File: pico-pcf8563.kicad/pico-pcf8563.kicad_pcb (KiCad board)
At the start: 2 copper layers, 21 x 18.6 mm, 13 parts, among them J1 Stemma-QT_Qwicc, J2 Ext_Conn, J4 Pico Pin 1-7, J5 Pico Pin 40-34, U1 PCF8563T, Y1 Crystal

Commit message: Rev2
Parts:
- added JP2: ~{INT}_Jumper, Jumper:SolderJumper-2_P1.3mm_Bridged_Pad1.0x1.5mm, B.Cu at (114.5, 109.5)
- added JP3: COUT_Jumper, Jumper:SolderJumper-2_P1.3mm_Bridged_Pad1.0x1.5mm, B.Cu at (114.5, 112.1)
- JP1: value VDD_SEL -> 3V3_Jumper; footprint Jumper:SolderJumper-3_P1.3mm_Bridged12_Pad1.0x1.5mm -> Jumper:SolderJumper-2_P1.3mm_Bridged_Pad1.0x1.5mm; moved to B.Cu
- moved R3 5.03 mm to (104.2, 112.4)
- moved R2 2.77 mm to (113.4, 100.5), turned to 90 degrees
- moved JP1 2.62 mm to (102.7, 108.7), turned to 90 degrees
- moved Y1 0.73 mm to (103.9, 102.2)
- moved C1 0.41 mm to (111.7, 100.0), turned to 180 degrees
- moved C2 0.38 mm to (106.1, 100.0)
- moved J1 0.33 mm to (108.9, 110.5)
- moved J2 0.33 mm to (102.5, 115.2)
- moved U1 0.33 mm to (108.9, 103.4)
- moved R1 0.26 mm to (115.2, 110.0)
- moved R4 0.20 mm to (115.2, 107.6)
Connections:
- C1 pad 1: VDD -> VCC
- J4 pad 6: unconnected-(J4-Pad6) -> /GP4
- J4 pad 7: unconnected-(J4-Pad7) -> /GP5
- JP1 pad 2: VDD -> VCC
- R2 pad 2: VDD -> VCC
- R3 pad 2: VDD -> VCC
- U1 pad 8: VDD -> VCC
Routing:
- net VDD: track 22.3 -> 0.00 mm
- net VCC: track 10.6 -> 32.1 mm, vias 0 -> 2
- net +3V3: track 3.07 -> 18.2 mm, vias 0 -> 1
- net /~{INT}: track 16.4 -> 25.7 mm
- net /SCL: track 19.9 -> 28.0 mm, vias 0 -> 1
- net GND: track 0.00 -> 7.26 mm, vias 0 -> 3
- net /COUT: track 15.7 -> 20.6 mm, vias 1 -> 2
- net /SDA: track 14.9 -> 19.4 mm
- net /GP4: track 0.00 -> 4.45 mm
- net /GP5: track 0.00 -> 4.23 mm
- added copper zone on B.Cu, net GND
- added copper zone on F.Cu, net GND

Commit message: Rev 3
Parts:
- J4: moved to B.Cu
- moved R1 4.33 mm to (114.6, 105.7), turned to -90 degrees
- moved R4 2.69 mm to (113.3, 105.7), turned to 90 degrees
- turned J4 to 180 degrees
- turned JP1 to -90 degrees
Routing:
- net +3V3: track 18.2 -> 45.4 mm, vias 1 -> 0
- net VCC: track 32.1 -> 57.8 mm, vias 2 -> 1
- net GND: track 7.26 -> 14.0 mm
- net /SCL: track 28.0 -> 25.6 mm
- net /SDA: track 19.4 -> 18.5 mm
- net /~{INT}: track 25.7 -> 25.1 mm
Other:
- board text added: "3V3 VCC"
- board text added: "COUT"
- board text added: "G"
- board text added: "SCL"
- board text added: "SDA"
- board text added: "VCC"
- board text added: "github.com/bablokb/ pcb-pico-pcf8563 Rev 3"
- board text added: "~{INT}"

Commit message: updated pcb from schematic for Rev3
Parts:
- JP2: value ~{INT}_Jumper -> COUT_Jumper
- JP3: value COUT_Jumper -> ~{INT}_Jumper
- R2: value 100K -> 10K
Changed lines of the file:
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@@
       (layerselection 0x00010fc_ffffffff)
       (disableapertmacros false)
-      (usegerberextensions false)
-      (usegerberattributes true)
-      (usegerberadvancedattributes true)
-      (creategerberjobfile true)
+      (usegerberextensions true)
+      (usegerberattributes false)
+      (usegerberadvancedattributes false)
+      (creategerberjobfile false)
       (svguseinch false)
       (svgprecision 6)
@@
       (psa4output false)
       (plotreference true)
-      (plotvalue true)
+      (plotvalue false)
       (plotinvisibletext false)
       (sketchpadsonfab false)
-      (subtractmaskfromsilk false)
+      (subtractmaskfromsilk true)
       (outputformat 1)
       (mirror false)
-      (drillshape 1)
+      (drillshape 0)
       (scaleselection 1)
-      (outputdirectory "")
+      (outputdirectory "../jlcpcb")
     )
   )
@@
     (descr "Resistor SMD 0402 (1005 Metric), square (rectangular) end terminal, IPC_7351 nominal, (Body size source: IPC-SM-782 page 72, https://www.pcb-3d.com/wordpress/wp-content/uploads/ipc-sm-782a_amendment_1_and_2.pdf), generated with kicad-footprint-generator")
     (tags "resistor")
-    (property "LCSC" "C25741")
+    (property "LCSC" "C25744")
     (property "Sheetfile" "pico-pcf8563.kicad_sch")
     (property "Sheetname" "")
@@
       (effects (font (size 1 1) (thickness 0.15)))
     )
-    (fp_text value "100K" (at 0 1.17 90) (layer "F.Fab") hide
+    (fp_text value "10K" (at 0 1.17 90) (layer "F.Fab") hide
       (effects (font (size 1 1) (thickness 0.15)))
     )
@@
     (property "Sheetname" "")
     (property "Value" "Stemma-QT_Qwicc")
-    (attr smd)
+    (attr smd exclude_from_pos_files)
     (fp_text reference "J1" (at 0 0) (layer "F.SilkS") hide
       (effects (font (size 1 1) (thickness 0.15)))
@@
     (pad "4" smd roundrect (at 1.5 -2) (size 0.6 1.55) (layers "F.Cu" "F.Paste" "F.Mask") (roundrect_rratio 0.25)
       (net 6 "/SCL") (pinfunction "SCL") (pintype "bidirectional"))
-    (pad "MP" smd roundrect (at -2.8 1.875) (size 1.2 1.8) (layers "F.Cu" "F.Paste" "F.Mask") (roundrect_rratio 0.208333))
-    (pad "MP" smd roundrect (at 2.8 1.875) (size 1.2 1.8) (layers "F.Cu" "F.Paste" "F.Mask") (roundrect_rratio 0.208333))
+    (pad "MP" smd roundrect (at -2.8 1.875) (size 1.2 1.8) (layers "F.Cu" "F.Paste" "F.Mask") (roundrect_rratio 0.2083333333))
+    (pad "MP" smd roundrect (at 2.8 1.875) (size 1.2 1.8) (layers "F.Cu" "F.Paste" "F.Mask") (roundrect_rratio 0.2083333333))
     (model "${KICAD6_3DMODEL_DIR}/Connector_JST.3dshapes/JST_SH_SM04B-SRSS-TB_1x04-1MP_P1.00mm_Horizontal.wrl"
       (offset (xyz 0 0 0))
@@
       (effects (font (size 1 1) (thickness 0.15)) (justify mirror))
     )
-    (fp_text value "~{INT}_Jumper" (at 0 -1.9) (layer "B.Fab") hide
+    (fp_text value "COUT_Jumper" (at 0 -1.9) (layer "B.Fab") hide
       (effects (font (size 1 1) (thickness 0.15)) (justify mirror))
     )
@@
       (effects (font (size 1 1) (thickness 0.15)) (justify mirror))
     )
-    (fp_text value "COUT_Jumper" (at 0 -1.9) (layer "B.Fab") hide
-      (effects (font (size 1 1) (thickness 0.15)) (justify mirror))
-    )
+    (fp_text value "~{INT}_Jumper" (at 0 -1.9) (layer "B.Fab") hide
+      (effects (font (size 1 1) (thickness 0.15)) (justify mirror))
+    )

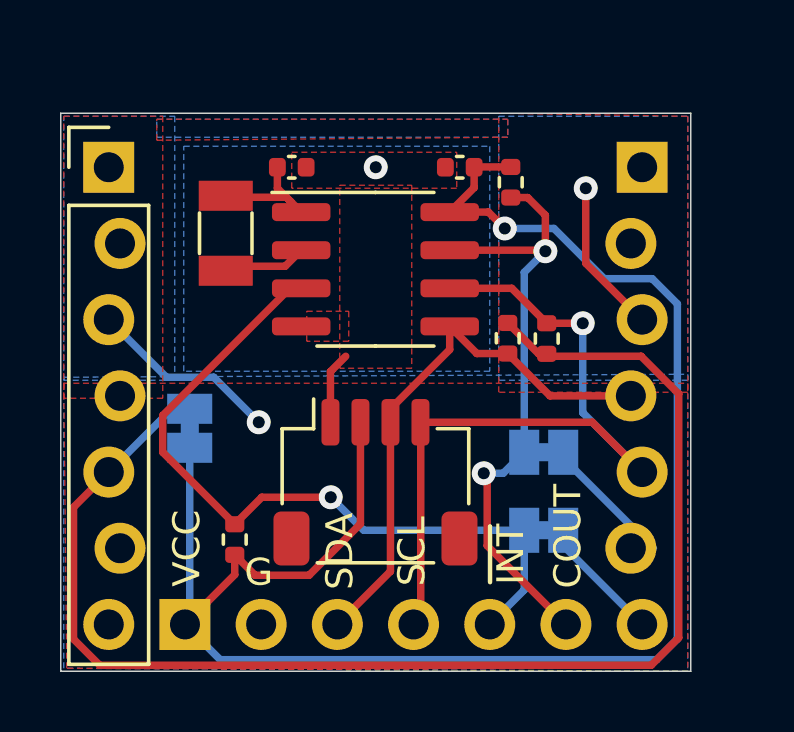
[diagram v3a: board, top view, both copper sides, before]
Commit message: Rev 4: swapped INT/CLKOUT. The latter is now on GP5
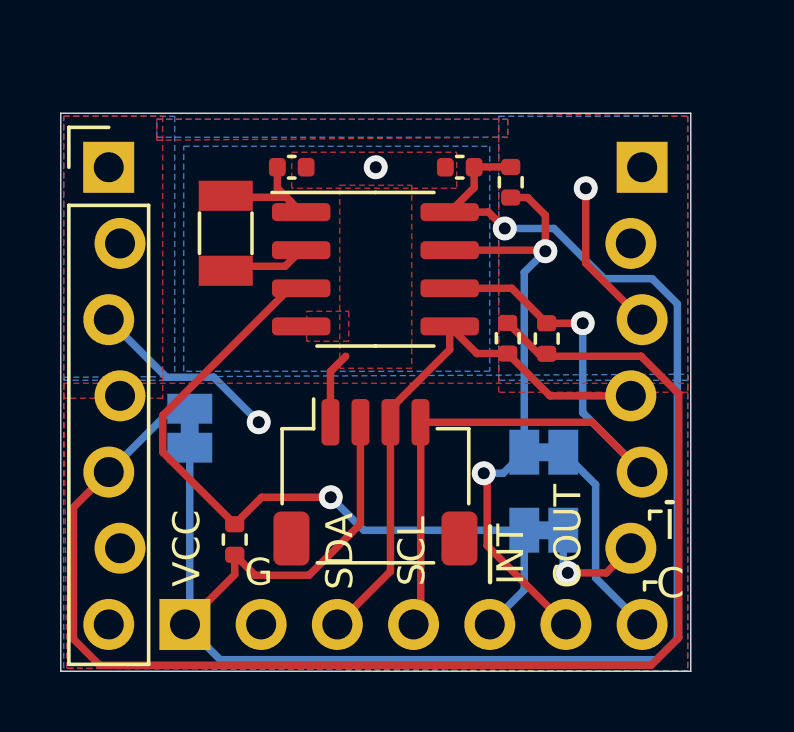
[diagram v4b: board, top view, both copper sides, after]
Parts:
- moved JP2 2.60 mm to (114.5, 112.1)
- moved JP3 2.60 mm to (114.5, 109.5)
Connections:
- JP2 pad 2: /COUT -> /~{INT}
- JP3 pad 2: /~{INT} -> /COUT
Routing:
- net /GP5: track 4.23 -> 6.83 mm
- net /GP4: track 4.45 -> 3.93 mm, vias 0 -> 1
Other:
- board text added: "C"
- board text added: "github.com/bablokb/ pcb-pico-pcf8563 Rev 4"
- board text added: "~{I}"
- board text removed: "github.com/bablokb/ pcb-pico-pcf8563 Rev 3"
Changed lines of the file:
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@@
     (descr "JST SH series connector, SM04B-SRSS-TB (http://www.jst-mfg.com/product/pdf/eng/eSH.pdf), generated with kicad-footprint-generator")
     (tags "connector JST SH top entry")
-    (property "Datasheet" "~")
+    (property "Datasheet" "")
     (property "Reference" "J1")
     (property "Sheetfile" "pico-pcf8563.kicad_sch")
     (property "Sheetname" "")
     (property "Value" "Stemma-QT_Qwicc")
-    (attr smd exclude_from_pos_files)
+    (property "exclude_from_bom" "")
+    (attr smd exclude_from_pos_files exclude_from_bom)
     (fp_text reference "J1" (at 0 0) (layer "F.SilkS") hide
       (effects (font (size 1 1) (thickness 0.15)))
@@
     (property "Sheetfile" "pico-pcf8563.kicad_sch")
     (property "Sheetname" "")
-    (attr through_hole)
+    (property "exclude_from_bom" "")
+    (attr through_hole exclude_from_pos_files exclude_from_bom)
     (fp_text reference "J5" (at 0.1 -2.54) (layer "F.SilkS") hide
       (effects (font (size 1 1) (thickness 0.15)))
@@
     (descr "Through hole straight pin header, 1x06, 2.54mm pitch, single row")
     (tags "Through hole pin header THT 1x06 2.54mm single row")
-    (property "Datasheet" "~")
+    (property "Datasheet" "")
     (property "Reference" "J2")
     (property "Sheetfile" "pico-pcf8563.kicad_sch")
     (property "Sheetname" "")
     (property "Value" "Ext_Conn")
-    (attr through_hole)
+    (property "exclude_from_bom" "")
+    (attr through_hole exclude_from_pos_files exclude_from_bom)
     (fp_text reference "J2" (at 0 2.33 90) (layer "B.SilkS") hide
       (effects (font (size 1 1) (thickness 0.15)) (justify mirror))
@@
       (effects (font (size 1 1) (thickness 0.15)) (justify mirror))
     )
-    (fp_text user "${REFERENCE}" (at 0 -6.35) (layer "B.Fab")
+    (fp_text user "${REFERENCE}" (at 0 -6.35) (layer "B.Fab") hide
       (effects (font (size 1 1) (thickness 0.15)) (justify mirror))
     )
@@
   )
   (footprint "Jumper:SolderJumper-2_P1.3mm_Bridged_Pad1.0x1.5mm" (layer "B.Cu")
-    (at 114.5 109.5 180)
+    (at 114.5 112.1 180)
     (descr "SMD Solder Jumper, 1x1.5mm Pads, 0.3mm gap, bridged with 1 copper strip")
     (tags "net tie solder jumper bridged")
     (property "Sheetfile" "pico-pcf8563.kicad_sch")
     (property "Sheetname" "")
-    (attr exclude_from_pos_files)
+    (property "exclude_from_bom" "")
+    (attr exclude_from_pos_files exclude_from_bom)
     (fp_text reference "JP2" (at 0 1.8) (layer "B.SilkS") hide
       (effects (font (size 1 1) (thickness 0.15)) (justify mirror))
@@
       (net 1 "/GP4") (pinfunction "A") (pintype "passive"))
     (pad "2" smd rect (at 0.65 0 180) (size 1 1.5) (layers "B.Cu" "B.Mask")
-      (net 8 "/COUT") (pinfunction "B") (pintype "passive"))
+      (net 7 "/~{INT}") (pinfunction "B") (pintype "passive"))
   )
   (footprint "Jumper:SolderJumper-2_P1.3mm_Bridged_Pad1.0x1.5mm" (layer "B.Cu")
-    (at 114.5 112.1 180)
+    (at 114.5 109.5 180)
     (descr "SMD Solder Jumper, 1x1.5mm Pads, 0.3mm gap, bridged with 1 copper strip")
     (tags "net tie solder jumper bridged")
     (property "Sheetfile" "pico-pcf8563.kicad_sch")
     (property "Sheetname" "")
-    (attr exclude_from_pos_files)
+    (property "exclude_from_bom" "")
+    (attr exclude_from_pos_files exclude_from_bom)
     (fp_text reference "JP3" (at 0 1.8) (layer "B.SilkS") hide
       (effects (font (size 1 1) (thickness 0.15)) (justify mirror))
@@
       (net 11 "/GP5") (pinfunction "A") (pintype "passive"))
     (pad "2" smd rect (at 0.65 0 180) (size 1 1.5) (layers "B.Cu" "B.Mask")
-      (net 7 "/~{INT}") (pinfunction "B") (pintype "passive"))
+      (net 8 "/COUT") (pinfunction "B") (pintype "passive"))
   )
   (footprint "user:Connector_1x7_no_solder" (layer "B.Cu")
@@
     (property "Sheetfile" "pico-pcf8563.kicad_sch")
     (property "Sheetname" "")
-    (attr through_hole)
+    (property "exclude_from_bom" "")
+    (attr through_hole exclude_from_pos_files exclude_from_bom)
     (fp_text reference "J4" (at 0.1 2.54) (layer "B.SilkS") hide
       (effects (font (size 1 1) (thickness 0.15)) (justify mirror))
@@
     (property "Sheetfile" "pico-pcf8563.kicad_sch")
     (property "Sheetname" "")
-    (attr exclude_from_pos_files)
+    (property "exclude_from_bom" "")
+    (attr exclude_from_pos_files exclude_from_bom)
     (fp_text reference "JP1" (at 0 1.8 90) (layer "B.SilkS") hide
       (effects (font (size 1 1) (thickness 0.15)) (justify mirror))
@@
       (net 4 "VCC") (pinfunction "B") (pintype "passive"))
   )
+  (gr_line (start 117.86 113.83) (end 117.86 114.09) (layer "F.SilkS") (width 0.12))
+  (gr_line (start 118.41 111.47) (end 118.03 111.47) (layer "F.SilkS") (width 0.12))
+  (gr_line (start 118.03 111.47) (end 118.03 111.73) (layer "F.SilkS") (width 0.12))
+  (gr_line (start 118.24 113.83) (end 117.86 113.83) (layer "F.SilkS") (width 0.12))
   (gr_rect (start 98.4 98.2) (end 119.4 116.8) (layer "Edge.Cuts") (width 0.05) (fill none))
-  (gr_text "github.com/bablokb/\npcb-pico-pcf8563\nRev 3" (at 116.2 100.8) (layer "B.SilkS")
+  (gr_text "github.com/bablokb/\npcb-pico-pcf8563\nRev 4" (at 116.2 100.8) (layer "B.SilkS")
     (effects (font (size 0.9 0.9) (thickness 0.15)) (justify left mirror))
   )
@@
     (effects (font (size 0.9 0.9) (thickness 0.15)))
   )
+  (gr_text "~{I}" (at 118.7 111.93) (layer "F.SilkS")
+    (effects (font (size 1 1) (thickness 0.15)))
+  )
   (gr_text "SDA" (at 107.7 112.8 90) (layer "F.SilkS")
     (effects (font (size 0.9 0.9) (thickness 0.15)))
   )
+  (gr_text "C" (at 118.72 113.87) (layer "F.SilkS")
+    (effects (font (size 1 1) (thickness 0.15)))
+  )
   (gr_text "G" (at 105 113.5) (layer "F.SilkS")
     (effects (font (size 0.9 0.9) (thickness 0.15)))
   )
-  (segment (start 115.15 109.69375) (end 118.15625 112.7) (width 0.25) (layer "B.Cu") (net 1))
-  (segment (start 115.15 109.5) (end 115.15 109.69375) (width 0.25) (layer "B.Cu") (net 1))
+  (segment (start 115.3 113.52) (end 116.58375 113.52) (width 0.25) (layer "F.Cu") (net 1))
+  (segment (start 116.58375 113.52) (end 117.40375 112.7) (width 0.25) (layer "F.Cu") (net 1))
+  (via (at 115.3 113.52) (size 0.8) (drill 0.4) (layers "F.Cu" "B.Cu") (net 1))
+  (segment (start 115.15 113.37) (end 115.3 113.52) (width 0.25) (layer "B.Cu") (net 1))
+  (segment (start 115.15 112.1) (end 115.15 113.37) (width 0.25) (layer "B.Cu") (net 1))
   (segment (start 107.39 106.81) (end 107.9 106.3) (width 0.25) (layer "F.Cu") (net 2))
   (segment (start 107.39 108.5) (end 107.39 106.81) (width 0.25) (layer "F.Cu") (net 2))
@@
   (segment (start 113.85 103.504) (end 114.554 102.8) (width 0.25) (layer "B.Cu") (net 8))
   (segment (start 113.15 110.2) (end 113.85 109.5) (width 0.25) (layer "B.Cu") (net 8))
-  (segment (start 115.15 112.1) (end 115.15 112.61) (width 0.25) (layer "B.Cu") (net 11))
-  (segment (start 115.15 112.61) (end 117.78 115.24) (width 0.25) (layer "B.Cu") (net 11))
+  (segment (start 116.22875 113.68875) (end 117.78 115.24) (width 0.25) (layer "B.Cu") (net 11))
+  (segment (start 116.22875 110.57875) (end 116.22875 113.68875) (width 0.25) (layer "B.Cu") (net 11))
+  (segment (start 115.15 109.5) (end 116.22875 110.57875) (width 0.25) (layer "B.Cu") (net 11))
   (segment (start 119 107.554549) (end 117.745451 106.3) (width 0.25) (layer "F.Cu") (net 15))
   (segment (start 119 115.681701) (end 119 107.554549) (width 0.25) (layer "F.Cu") (net 15))
